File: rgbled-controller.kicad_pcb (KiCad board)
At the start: 2 copper layers, 65.1 x 43.5 mm, 23 parts, among them IC1 ME6211C33M5G-N, J1 PROG_HDR, J2 IC2_Header, J3 Power In, J4 LED_OUT, Q1 UMH3N, Q2 2N7002, SW1 Reset, SW2 Flash, U1 ESP-12F

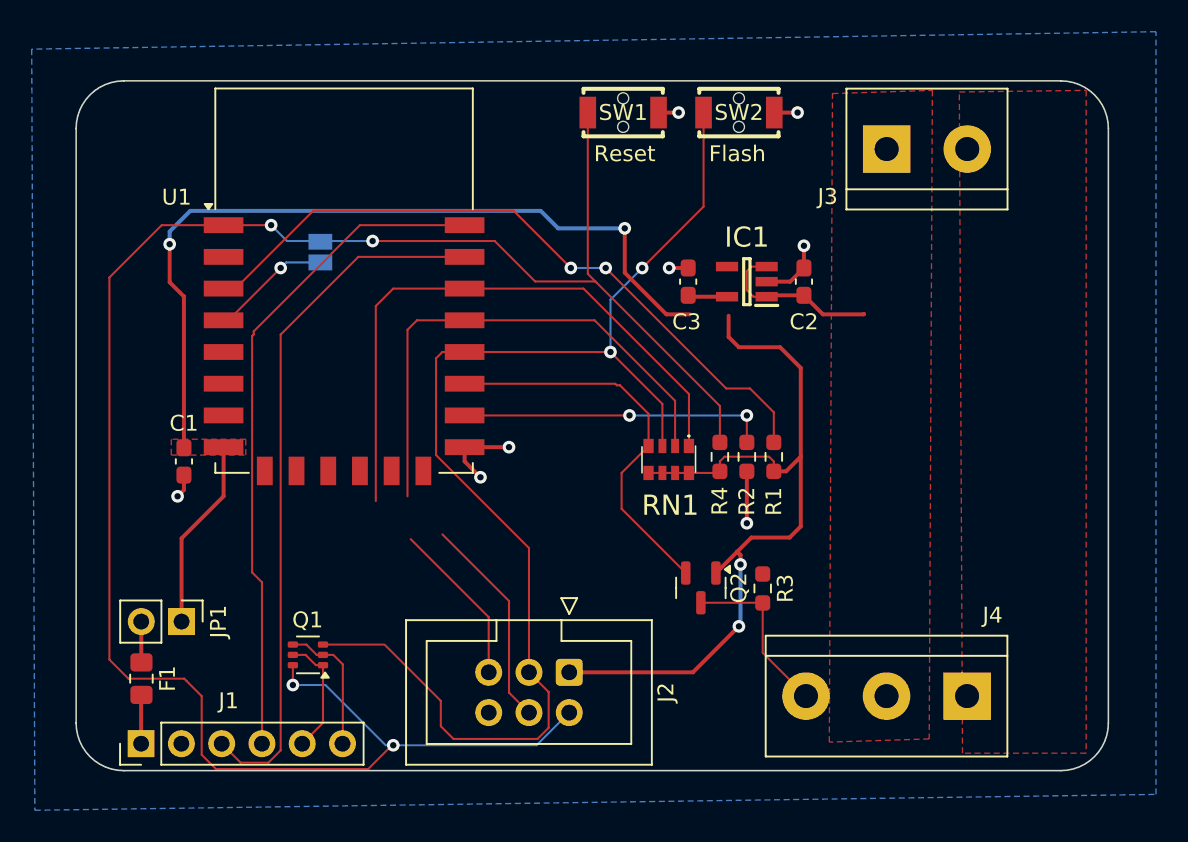
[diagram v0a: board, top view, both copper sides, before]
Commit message: added 3 mounting points and crc check complete
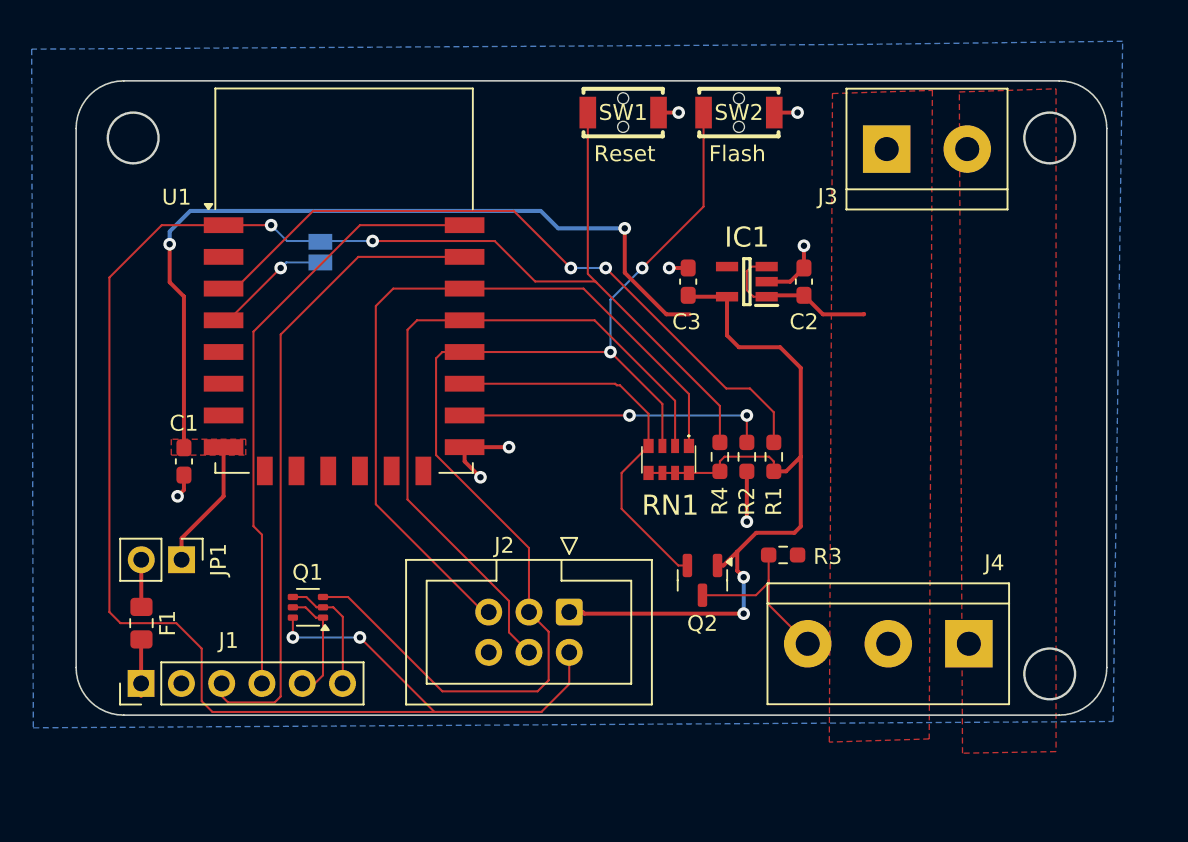
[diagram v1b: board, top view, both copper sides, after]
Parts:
- moved JP1 3.90 mm to (103.5, 88.8)
- moved J1 3.80 mm to (101.0, 96.6)
- moved J2 3.80 mm to (128.0, 92.1)
- moved F1 3.50 mm to (101.0, 92.8)
- moved J4 3.30 mm to (153.2, 94.1)
- moved Q1 3.00 mm to (111.5, 91.8)
- moved R3 2.47 mm to (141.5, 88.5), turned to 180 degrees
- moved Q2 0.49 mm to (136.4, 90.1)
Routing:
- net ~{RESET}: track 126.4 -> 134.1 mm
- net +3V3: track 117.8 -> 113.3 mm
- net /GPIO3_RX: track 44.4 -> 40.5 mm
- net ~{GPIO0_INT_FLASH}: track 80.1 -> 76.2 mm
- net /GPIO4_TX: track 42.4 -> 39.3 mm
- net GPIO4_SDA: track 46.1 -> 45.6 mm
- net /3v3PROG: track 3.08 -> 3.58 mm
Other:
- board size 65.1 x 43.5 mm -> 65 x 40 mm

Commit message: changed board layout and added spare pins
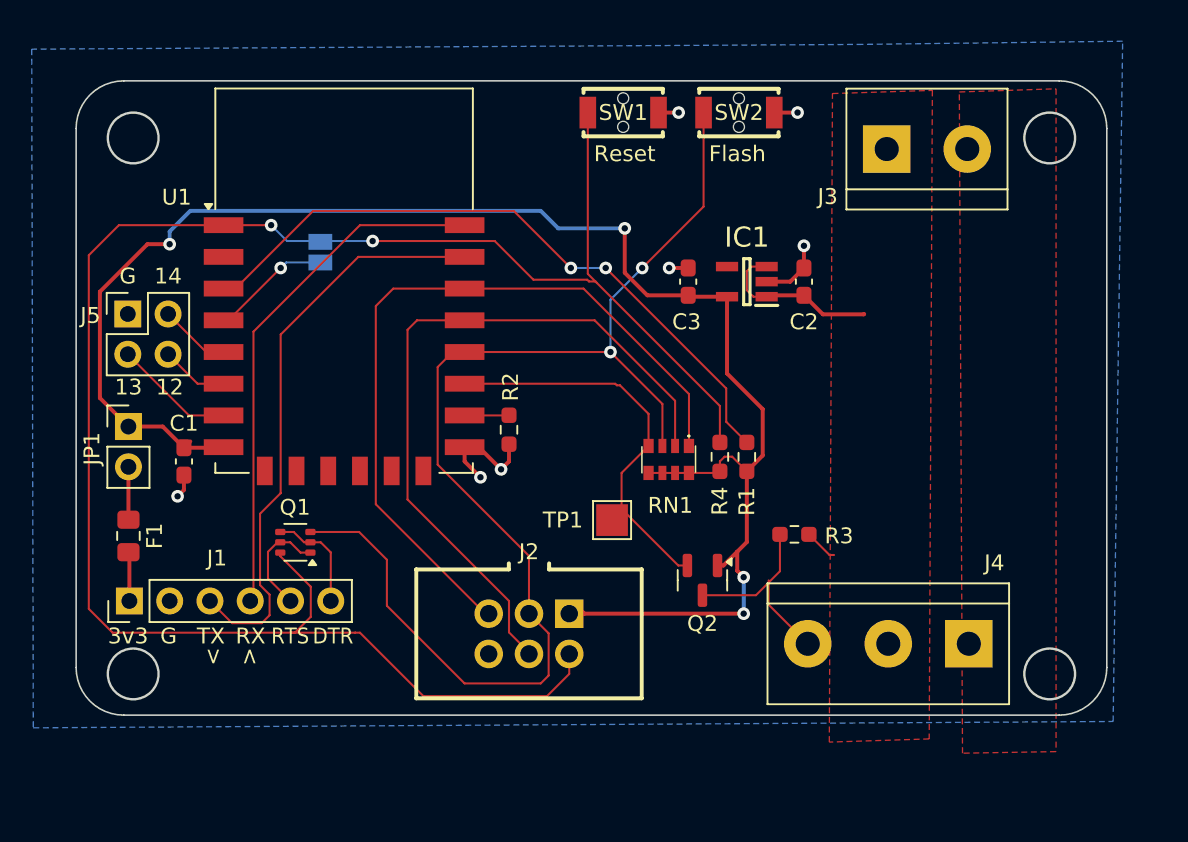
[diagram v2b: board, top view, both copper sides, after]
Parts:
- added J5: PinHeader_2x02_P2.54mm_Vertical, Connector_PinHeader_2.54mm:PinHeader_2x02_P2.54mm_Vertical, F.Cu at (100.2, 73.3)
- added TP1: LED_CTRL, TestPoint:TestPoint_Pad_2.0x2.0mm, F.Cu at (130.7, 86.3)
- J2: footprint Connector_IDC:IDC-Header_2x03_P2.54mm_Vertical -> Chof747 Connectors:HDR-TH_6P-P2.54-V-F-R2-C3-S2.54-4
- moved G*** 173.2 mm to (157.4, 73.9)
- moved R2 15.1 mm to (124.2, 80.6)
- moved JP1 9.04 mm to (100.2, 80.4), turned to 0 degrees
- moved F1 5.56 mm to (100.2, 87.3)
- moved J1 5.25 mm to (100.3, 91.4)
- moved Q1 4.18 mm to (110.7, 87.7)
- moved J2 2.89 mm to (125.5, 93.5), turned to 180 degrees
- moved R1 1.70 mm to (139.2, 82.3)
- moved R3 1.48 mm to (142.2, 87.2)
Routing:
- net Net-(U1-GPIO15): track 19.5 -> 2.81 mm, vias 2 -> 0
- net ~{RESET}: track 134.1 -> 121.7 mm, vias 4 -> 2
- net +3V3: track 113.3 -> 104.3 mm
- net unconnected-(U1-GPIO13-Pad7): track 0.00 -> 7.64 mm
- net /GPIO4_TX: track 39.3 -> 33.2 mm
- net unconnected-(U1-GPIO14-Pad5): track 0.00 -> 4.49 mm
- net unconnected-(U1-GPIO12-Pad6): track 0.00 -> 4.27 mm
- net /GPIO3_RX: track 40.5 -> 36.7 mm
- net ~{GPIO0_INT_FLASH}: track 76.2 -> 79.3 mm
- net +5V: track 10.7 -> 12.8 mm
- net DTR: track 8.68 -> 6.78 mm
- net OUT_LED_CTRL: track 11.3 -> 12.9 mm
- net Net-(U1-EN): track 43.9 -> 42.3 mm
- net GND: track 17.8 -> 16.5 mm, vias 8 -> 7
- net RTS: track 7.66 -> 6.88 mm
- removed copper zone on F.Cu, net +3V3
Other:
- outline, holes or cut-outs redrawn
- board text added: "12"
- board text added: "13"
- board text added: "14"
- board text added: "3v3"
- board text added: ">"
- board text added: "DTR"
- board text added: "G"
- board text added: "RGB-Led Controll Board v1.0 chof (c)2025"
- board text added: "RTS"
- board text added: "RX"
- board text added: "TX"
